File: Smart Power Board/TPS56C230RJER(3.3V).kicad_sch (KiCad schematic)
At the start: 19 parts, among them IC3 TPS56C230RJER

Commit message: Feat[SmartPowerBoard]: MCU Development
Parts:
- renumbered IC3 to U5
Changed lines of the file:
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@@
 		(on_board yes)
 		(dnp no)
-		(property "Reference" "IC3"
+		(property "Reference" "U5"
 			(at 163.322 119.634 0)
 			(effects
@@
 			(project "SmartPowerBoard"
 				(path "/787a0061-c9d5-4e8d-b49f-b4e75e937f85/09ce01d1-d55d-4db1-b029-11fc4085741e"
-					(reference "IC3")
+					(reference "U5")
 					(unit 1)
 				)

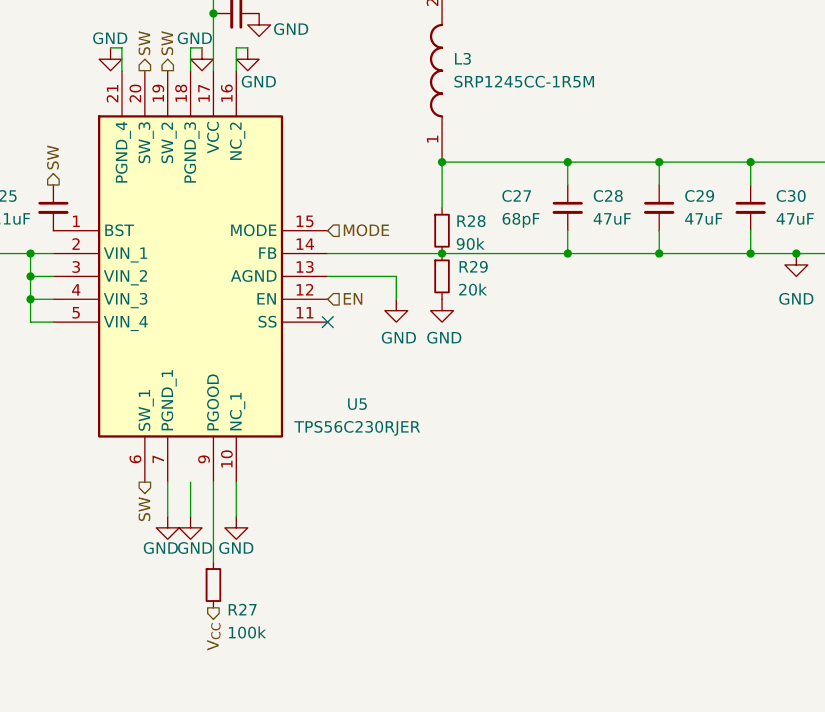
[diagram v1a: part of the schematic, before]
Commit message: Feat[SmartPowerBoard]:Starting Board Layout
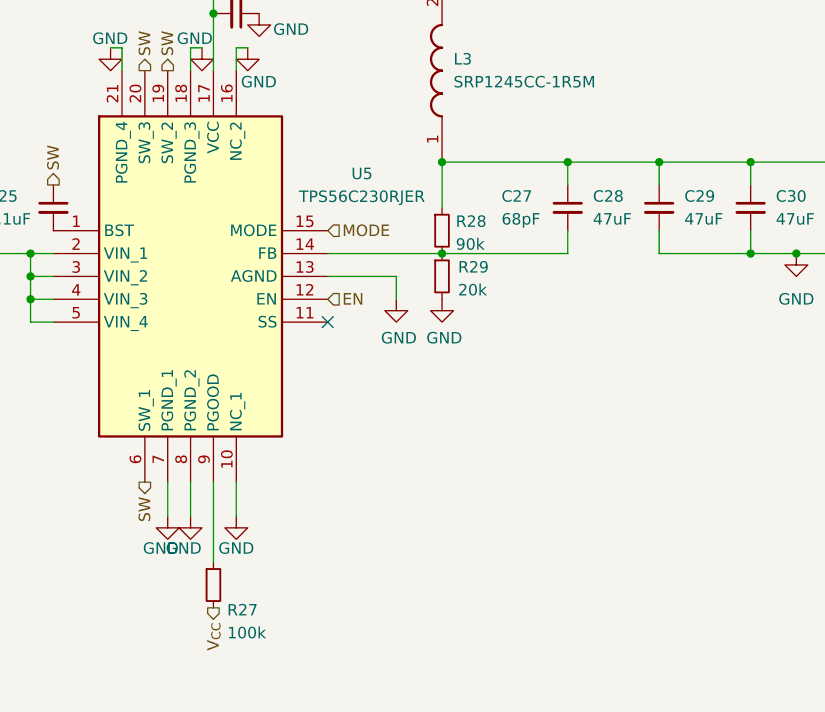
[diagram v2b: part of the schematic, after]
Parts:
- C22, C23, C24, C25, C26, C28, C29, C30, C31: footprint (none) -> Capacitor_SMD:C_0402_1005Metric
- C27: footprint (none) -> Capacitor_SMD:C_0201_0603Metric
- R22, R24, R25, R26, R27, R28, R29: footprint (none) -> Resistor_SMD:R_0402_1005Metric
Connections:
- net GND: now also U5.8 (PGND_2); no longer C27.2, R28.2, R29.1, U5.14 (FB)
- new net: C27.2, R28.2, R29.1, U5.14 (FB)

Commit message: Feat[SmartPowerBoard]: Layout
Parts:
- removed L3: SRP1245CC-1R5M, INDPM135125X500N, symbol SRP1245CC-1R5M:SRP1245CC-1R5M
- added L2: IHLP4040DZER1R5M01, INDPM108103X400N, symbol IHLP4040DZER1R5M01:IHLP4040DZER1R5M01
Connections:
- net SW: now also L2.2
- net V_{OUT}: now also L2.1
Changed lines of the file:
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@@
+	)
+	(symbol
+		(lib_id "IHLP4040DZER1R5M01:IHLP4040DZER1R5M01")
+		(at 172.72 92.71 90)
+		(unit 1)
+		(exclude_from_sim no)
+		(in_bom yes)
+		(on_board yes)
+		(dnp no)
+		(fields_autoplaced yes)
+		(property "Reference" "L2"
+			(at 173.99 81.2799 90)
+			(effects
+				(font
+					(size 1.27 1.27)
+				)
+				(justify right)
+			)
+		)
+		(property "Value" "IHLP4040DZER1R5M01"
+			(at 173.99 83.8199 90)
+			(effects
+				(font
+					(size 1.27 1.27)
+				)
+				(justify right)
+			)
+		)
+		(property "Footprint" "INDPM108103X400N"
+			(at 268.91 76.2 0)
+			(effects
+				(font
+					(size 1.27 1.27)
+				)
+				(justify left top)
+				(hide yes)
+			)
+		)
+		(property "Datasheet" "https://componentsearchengine.com/Datasheets/2/IHLP4040DZER1R5M01.pdf"
+			(at 368.91 76.2 0)
+			(effects
+				(font
+					(size 1.27 1.27)
+				)
+				(justify left top)
+				(hide yes)
+			)
+		)
+		(property "Description" "Fixed Inductors 1.5uH 20%"
+			(at 172.72 92.71 0)
+			(effects
+				(font
+					(size 1.27 1.27)
+				)
+				(hide yes)
+			)
+		)
+		(property "Height" "4"
+			(at 568.91 76.2 0)
+			(effects
+				(font
+					(size 1.27 1.27)
+				)
+				(justify left top)
+				(hide yes)
+			)
+		)
+		(property "Manufacturer_Name" "Vishay"
+			(at 668.91 76.2 0)
+			(effects
+				(font
+					(size 1.27 1.27)
+				)
+				(justify left top)
+				(hide yes)
+			)
+		)
+		(property "Manufacturer_Part_Number" "IHLP4040DZER1R5M01"
+			(at 768.91 76.2 0)
+			(effects
+				(font
+					(size 1.27 1.27)
+				)
+				(justify left top)
+				(hide yes)
+			)
+		)
+		(property "Arrow Part Number" "IHLP4040DZER1R5M01"
+			(at 868.91 76.2 0)
+			(effects
+				(font
+					(size 1.27 1.27)
+				)
+				(justify left top)
+				(hide yes)
+			)
+		)
+		(property "Arrow Price/Stock" "https://www.arrow.com/en/products/ihlp4040dzer1r5m01/vishay?region=nac"
+			(at 968.91 76.2 0)
+			(effects
+				(font
+					(size 1.27 1.27)
+				)
+				(justify left top)
+				(hide yes)
+			)
+		)
+		(pin "2"
+		)
+		(pin "1"
+		)
+		(instances
+			(project "SmartPowerBoard"
+				(path "/787a0061-c9d5-4e8d-b49f-b4e75e937f85/09ce01d1-d55d-4db1-b029-11fc4085741e"
+					(reference "L2")
+					(unit 1)
+				)
+			)
+		)
 	)
 	(symbol
@@
 					(unit 1)
 				)
-			)
-		)
-	)
-	(symbol
-		(lib_id "SRP1245CC-1R5M:SRP1245CC-1R5M")
-		(at 172.72 92.71 90)
-		(unit 1)
-		(exclude_from_sim no)
-		(in_bom yes)
-		(on_board yes)
-		(dnp no)
-		(fields_autoplaced yes)
-		(property "Reference" "L3"
-			(at 173.99 81.2799 90)
-			(effects
-				(font
-					(size 1.27 1.27)
-				)
-				(justify right)
-			)
-		)
-		(property "Value" "SRP1245CC-1R5M"
-			(at 173.99 83.8199 90)
-			(effects
-				(font
-					(size 1.27 1.27)
-				)
-				(justify right)
-			)
-		)
-		(property "Footprint" "INDPM135125X500N"
-			(at 268.91 76.2 0)
-			(effects
-				(font
-					(size 1.27 1.27)
-				)
-				(justify left top)
-				(hide yes)
-			)
-		)
-		(property "Datasheet" "https://www.bourns.com/docs/Product-Datasheets/SRP1245CC.pdf"
-			(at 368.91 76.2 0)
-			(effects
-				(font
-					(size 1.27 1.27)
-				)
-				(justify left top)
-				(hide yes)
-			)
-		)
-		(property "Description" "Ind,13.5x12.5x4.8mm,1.5uH+/-20%,27A,shd"
-			(at 172.72 92.71 0)
-			(effects
-				(font
-					(size 1.27 1.27)
-				)
-				(hide yes)
-			)
-		)
-		(property "Height" "5"
-			(at 568.91 76.2 0)
-			(effects
-				(font
-					(size 1.27 1.27)
-				)
-				(justify left top)
-				(hide yes)
-			)
-		)
-		(property "Mouser Part Number" "652-SRP1245CC-1R5M"
-			(at 668.91 76.2 0)
-			(effects
-				(font
-					(size 1.27 1.27)
-				)
-				(justify left top)
-				(hide yes)
-			)
-		)
-		(property "Mouser Price/Stock" "https://www.mouser.co.uk/ProductDetail/Bourns/SRP1245CC-1R5M?qs=1Kr7Jg1SGW995LB%2Fs%252BVjpg%3D%3D"
-			(at 768.91 76.2 0)
-			(effects
-				(font
-					(size 1.27 1.27)
-				)
-				(justify left top)
-				(hide yes)
-			)
-		)
-		(property "Manufacturer_Name" "Bourns"
-			(at 868.91 76.2 0)
-			(effects
-				(font
-					(size 1.27 1.27)
-				)
-				(justify left top)
-				(hide yes)
-			)
-		)
-		(property "Manufacturer_Part_Number" "SRP1245CC-1R5M"
-			(at 968.91 76.2 0)
-			(effects
-				(font
-					(size 1.27 1.27)
-				)
-				(justify left top)
-				(hide yes)
-			)
-		)
-		(pin "2"
-		)
-		(pin "1"
-		)
-		(instances
-			(project "SmartPowerBoard"
-				(path "/787a0061-c9d5-4e8d-b49f-b4e75e937f85/09ce01d1-d55d-4db1-b029-11fc4085741e"
-					(reference "L3")
-					(unit 1)
-				)

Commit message: Feat[SmartPowerBoard]: Mid-Progress Update
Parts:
- removed L2: IHLP4040DZER1R5M01, INDPM108103X400N, symbol IHLP4040DZER1R5M01:IHLP4040DZER1R5M01
- added L2: SRR0735HA-151M, SRR0735HA151M, symbol SRR0735HA-151M:SRR0735HA-151M
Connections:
- net SW: now also L2.2
- net V_{OUT}: now also L2.1
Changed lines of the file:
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@@
+	)
+	(junction
+		(at 172.72 92.71)
+		(diameter 0)
+		(color 0 0 0 0)
 	)
 	(junction
@@
 	(junction
 		(at 227.33 92.71)
-		(diameter 0)
-		(color 0 0 0 0)
-	)
-	(junction
-		(at 172.72 92.71)
 		(diameter 0)
 		(color 0 0 0 0)
@@
 				(path "/787a0061-c9d5-4e8d-b49f-b4e75e937f85/09ce01d1-d55d-4db1-b029-11fc4085741e"
 					(reference "R24")
+					(unit 1)
+				)
+			)
+		)
+	)
+	(symbol
+		(lib_id "SRR0735HA-151M:SRR0735HA-151M")
+		(at 172.72 92.71 90)
+		(unit 1)
+		(exclude_from_sim no)
+		(in_bom yes)
+		(on_board yes)
+		(dnp no)
+		(fields_autoplaced yes)
+		(property "Reference" "L2"
+			(at 173.99 81.2799 90)
+			(effects
+				(font
+					(size 1.27 1.27)
+				)
+				(justify right)
+			)
+		)
+		(property "Value" "SRR0735HA-151M"
+			(at 173.99 83.8199 90)
+			(effects
+				(font
+					(size 1.27 1.27)
+				)
+				(justify right)
+			)
+		)
+		(property "Footprint" "SRR0735HA151M"
+			(at 268.91 76.2 0)
+			(effects
+				(font
+					(size 1.27 1.27)
+				)
+				(justify left top)
+				(hide yes)
+			)
+		)
+		(property "Datasheet" "https://www.bourns.com/docs/Product-Datasheets/SRR0735HA.pdf"
+			(at 368.91 76.2 0)
+			(effects
+				(font
+					(size 1.27 1.27)
+				)
+				(justify left top)
+				(hide yes)
+			)
+		)
+		(property "Description" "Ind,7.3x7.3x3.5,150uH+/-20%,0.47A,shd"
+			(at 172.72 92.71 0)
+			(effects
+				(font
+					(size 1.27 1.27)
+				)
+				(hide yes)
+			)
+		)
+		(property "Height" "3.7"
+			(at 568.91 76.2 0)
+			(effects
+				(font
+					(size 1.27 1.27)
+				)
+				(justify left top)
+				(hide yes)
+			)
+		)
+		(property "Mouser Part Number" "652-SRR0735HA-151M"
+			(at 668.91 76.2 0)
+			(effects
+				(font
+					(size 1.27 1.27)
+				)
+				(justify left top)
+				(hide yes)
+			)
+		)
+		(property "Mouser Price/Stock" "https://www.mouser.co.uk/ProductDetail/Bourns/SRR0735HA-151M?qs=mELouGlnn3dWb%2Fm7RDXtBg%3D%3D"
+			(at 768.91 76.2 0)
+			(effects
+				(font
+					(size 1.27 1.27)
+				)
+				(justify left top)
+				(hide yes)
+			)
+		)
+		(property "Manufacturer_Name" "Bourns"
+			(at 868.91 76.2 0)
+			(effects
+				(font
+					(size 1.27 1.27)
+				)
+				(justify left top)
+				(hide yes)
+			)
+		)
+		(property "Manufacturer_Part_Number" "SRR0735HA-151M"
+			(at 968.91 76.2 0)
+			(effects
+				(font
+					(size 1.27 1.27)
+				)
+				(justify left top)
+				(hide yes)
+			)
+		)
+		(pin "2"
+		)
+		(pin "1"
+		)
+		(instances
+			(project "SmartPowerBoard"
+				(path "/787a0061-c9d5-4e8d-b49f-b4e75e937f85/09ce01d1-d55d-4db1-b029-11fc4085741e"
+					(reference "L2")
 					(unit 1)
 				)
@@
 					(unit 1)
 				)
-			)
-		)
-	)
-	(symbol
-		(lib_id "IHLP4040DZER1R5M01:IHLP4040DZER1R5M01")
-		(at 172.72 92.71 90)
-		(unit 1)
-		(exclude_from_sim no)
-		(in_bom yes)
-		(on_board yes)
-		(dnp no)
-		(fields_autoplaced yes)
-		(property "Reference" "L2"
-			(at 173.99 81.2799 90)
-			(effects
-				(font
-					(size 1.27 1.27)
-				)
-				(justify right)
-			)
-		)
-		(property "Value" "IHLP4040DZER1R5M01"
-			(at 173.99 83.8199 90)
-			(effects
-				(font
-					(size 1.27 1.27)
-				)
-				(justify right)
-			)
-		)
-		(property "Footprint" "INDPM108103X400N"
-			(at 268.91 76.2 0)
-			(effects
-				(font
-					(size 1.27 1.27)
-				)
-				(justify left top)
-				(hide yes)
-			)
-		)
-		(property "Datasheet" "https://componentsearchengine.com/Datasheets/2/IHLP4040DZER1R5M01.pdf"
-			(at 368.91 76.2 0)
-			(effects
-				(font
-					(size 1.27 1.27)
-				)
-				(justify left top)
-				(hide yes)
-			)
-		)
-		(property "Description" "Fixed Inductors 1.5uH 20%"
-			(at 172.72 92.71 0)
-			(effects
-				(font
-					(size 1.27 1.27)
-				)
-				(hide yes)
-			)
-		)
-		(property "Height" "4"
-			(at 568.91 76.2 0)
-			(effects
-				(font
-					(size 1.27 1.27)
-				)
-				(justify left top)
-				(hide yes)
-			)
-		)
-		(property "Manufacturer_Name" "Vishay"
-			(at 668.91 76.2 0)
-			(effects
-				(font
-					(size 1.27 1.27)
-				)
-				(justify left top)
-				(hide yes)
-			)
-		)
-		(property "Manufacturer_Part_Number" "IHLP4040DZER1R5M01"
-			(at 768.91 76.2 0)
-			(effects
-				(font
-					(size 1.27 1.27)
-				)
-				(justify left top)
-				(hide yes)
-			)
-		)
-		(property "Arrow Part Number" "IHLP4040DZER1R5M01"
-			(at 868.91 76.2 0)
-			(effects
-				(font
-					(size 1.27 1.27)
-				)
-				(justify left top)
-				(hide yes)
-			)
-		)
-		(property "Arrow Price/Stock" "https://www.arrow.com/en/products/ihlp4040dzer1r5m01/vishay?region=nac"
-			(at 968.91 76.2 0)
-			(effects
-				(font
-					(size 1.27 1.27)
-				)
-				(justify left top)
-				(hide yes)
-			)
-		)
-		(pin "2"
-		)
-		(pin "1"
-		)
-		(instances
-			(project "SmartPowerBoard"
-				(path "/787a0061-c9d5-4e8d-b49f-b4e75e937f85/09ce01d1-d55d-4db1-b029-11fc4085741e"
-					(reference "L2")
-					(unit 1)
-				)
